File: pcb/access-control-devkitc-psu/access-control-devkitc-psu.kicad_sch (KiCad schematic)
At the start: 5 parts, among them J1 Conn_01x02_Socket

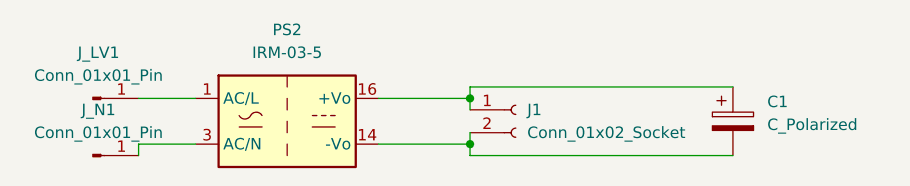
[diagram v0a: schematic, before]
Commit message: Option for 5v out on the other side
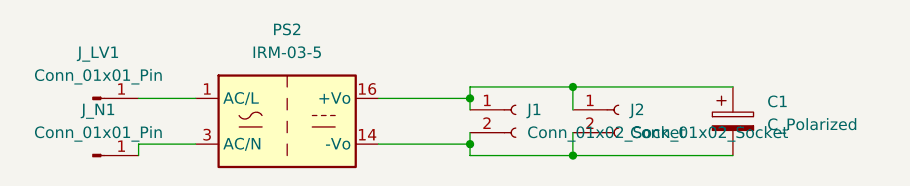
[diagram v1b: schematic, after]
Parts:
- added J2: Conn_01x02_Socket, Connector_PinHeader_2.54mm:PinHeader_1x02_P2.54mm_Vertical, symbol Connector:Conn_01x02_Socket
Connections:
- net at C1.1, J1.1 (Pin_1), PS2.16 (+Vo): now also J2.1 (Pin_1)
- net at C1.2, J1.2 (Pin_2), PS2.14 (-Vo): now also J2.2 (Pin_2)
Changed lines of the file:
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@@
 	(paper "A4")
+	(junction
+		(at 130.81 83.82)
+		(diameter 0)
+		(color 0 0 0 0)
+	)
 	(junction
 		(at 119.38 90.17)
@@
 		(color 0 0 0 0)
 	)
+	(junction
+		(at 130.81 91.44)
+		(diameter 0)
+		(color 0 0 0 0)
+	)
 	(wire
 		(pts
@@
 	(wire
 		(pts
+			(xy 130.81 83.82) (xy 119.38 83.82)
+		)
+		(stroke
+			(width 0)
+			(type default)
+		)
+	)
+	(wire
+		(pts
 			(xy 119.38 90.17) (xy 119.38 88.9)
 		)
@@
 	(wire
 		(pts
-			(xy 148.59 83.82) (xy 119.38 83.82)
+			(xy 148.59 83.82) (xy 130.81 83.82)
+		)
+		(stroke
+			(width 0)
+			(type default)
+		)
+	)
+	(wire
+		(pts
+			(xy 130.81 91.44) (xy 119.38 91.44)
 		)
 		(stroke
@@
 	(wire
 		(pts
-			(xy 148.59 91.44) (xy 119.38 91.44)
+			(xy 148.59 91.44) (xy 130.81 91.44)
 		)
 		(stroke
@@
 		(pts
 			(xy 82.55 85.09) (xy 88.9 85.09)
+		)
+		(stroke
+			(width 0)
+			(type default)
+		)
+	)
+	(wire
+		(pts
+			(xy 130.81 83.82) (xy 130.81 86.36)
+		)
+		(stroke
+			(width 0)
+			(type default)
+		)
+	)
+	(wire
+		(pts
+			(xy 130.81 88.9) (xy 130.81 91.44)
 		)
 		(stroke
@@
 					(unit 1)
 				)
+			)
+		)
+	)
+	(symbol
+		(lib_id "Connector:Conn_01x02_Socket")
+		(at 135.89 86.36 0)
+		(unit 1)
+		(exclude_from_sim no)
+		(in_bom yes)
+		(on_board yes)
+		(dnp no)
+		(fields_autoplaced yes)
+		(property "Reference" "J2"
+			(at 137.16 86.3599 0)
+			(effects
+				(font
+					(size 1.27 1.27)
+				)
+				(justify left)
+			)
+		)
+		(property "Value" "Conn_01x02_Socket"
+			(at 137.16 88.8999 0)
+			(effects
+				(font
+					(size 1.27 1.27)
+				)
+				(justify left)
+			)
+		)
+		(property "Footprint" "Connector_PinHeader_2.54mm:PinHeader_1x02_P2.54mm_Vertical"
+			(at 135.89 86.36 0)
+			(effects
+				(font
+					(size 1.27 1.27)
+				)
+				(hide yes)
+			)
+		)
+		(property "Datasheet" "~"
+			(at 135.89 86.36 0)
+			(effects
+				(font
+					(size 1.27 1.27)
+				)
+				(hide yes)
+			)
+		)
+		(property "Description" "Generic connector, single row, 01x02, script generated"
+			(at 135.89 86.36 0)
+			(effects
+				(font
+					(size 1.27 1.27)
+				)
+				(hide yes)
+			)
+		)
+		(pin "1"
+		)
+		(pin "2"
+		)
+		(instances
+			(project "access-control-devkitc-psu"
+				(path "/d592ddd9-ec8a-4205-8c1a-840537a83eb3"
+					(reference "J2")
+					(unit 1)
+				)
